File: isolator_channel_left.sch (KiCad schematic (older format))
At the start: 44 parts, among them U301 NE5532, U302 NE5532, U303 NE5532, U304 NE5532, U305 NE5532, U306 NE5532, U307 NE5532, U308 NE5532

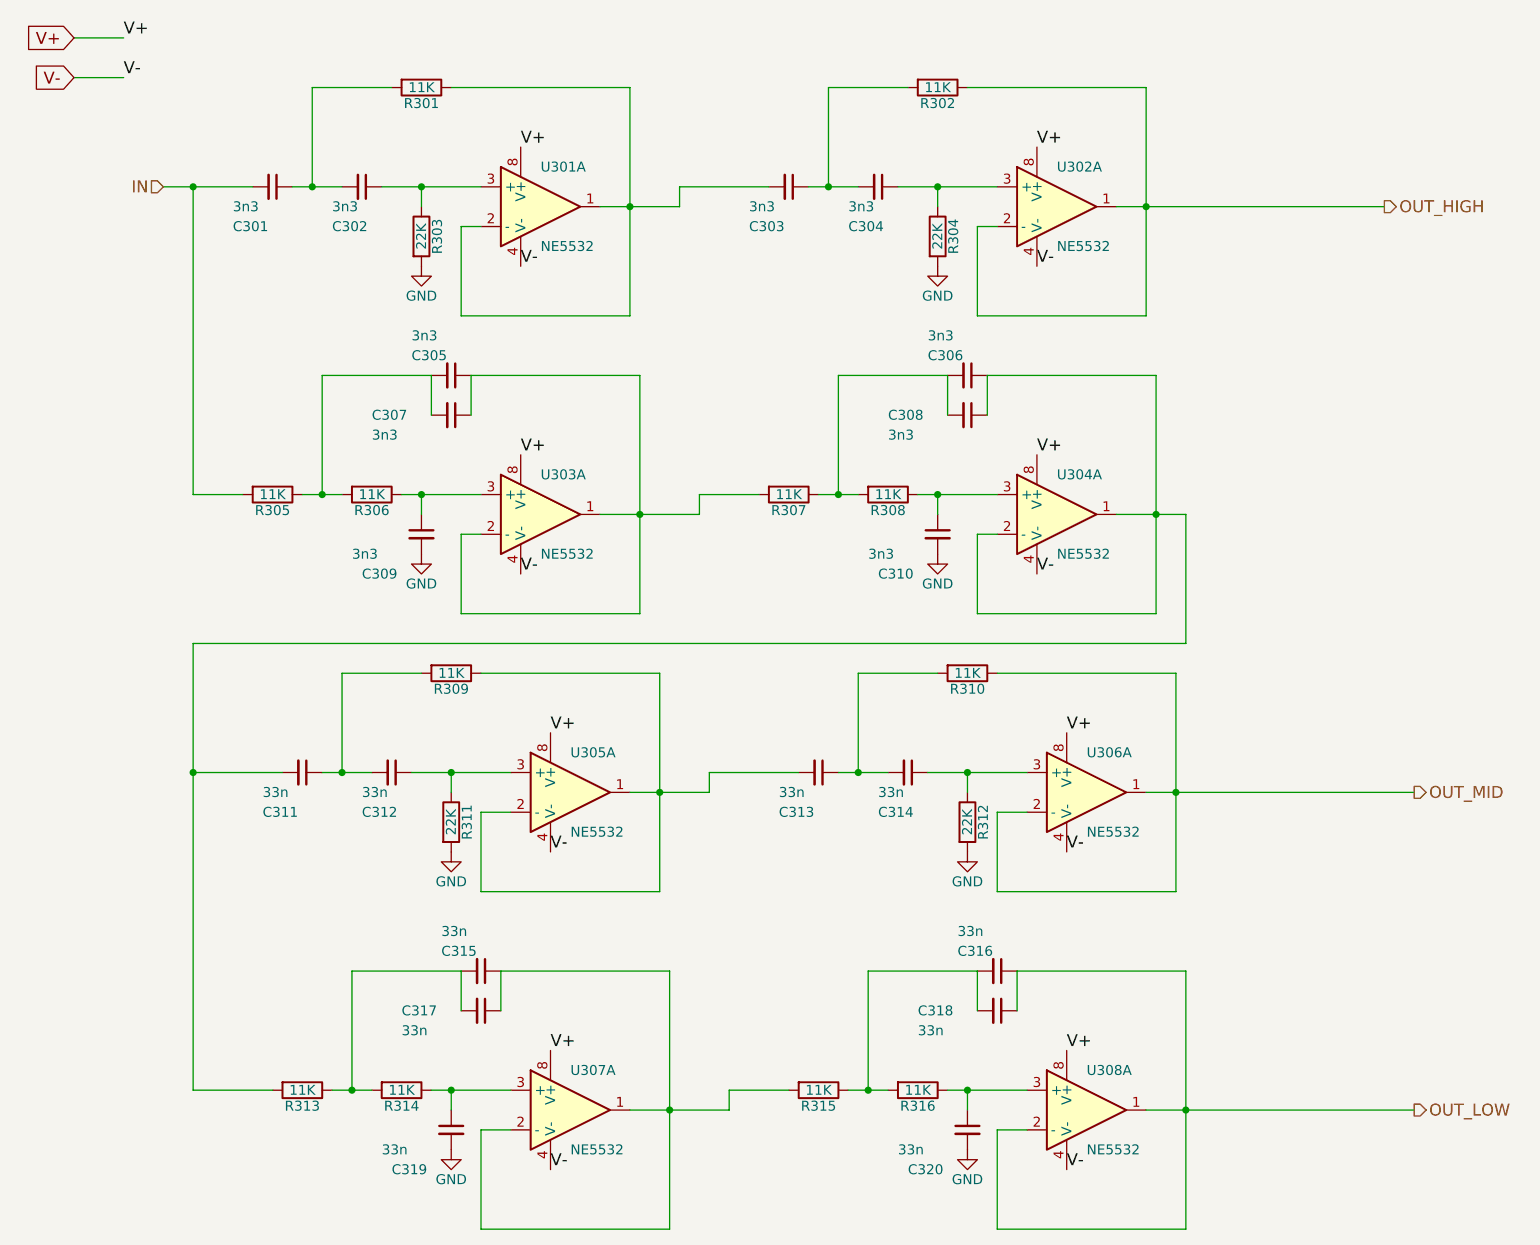
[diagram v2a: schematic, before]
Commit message: Updated components references and properties
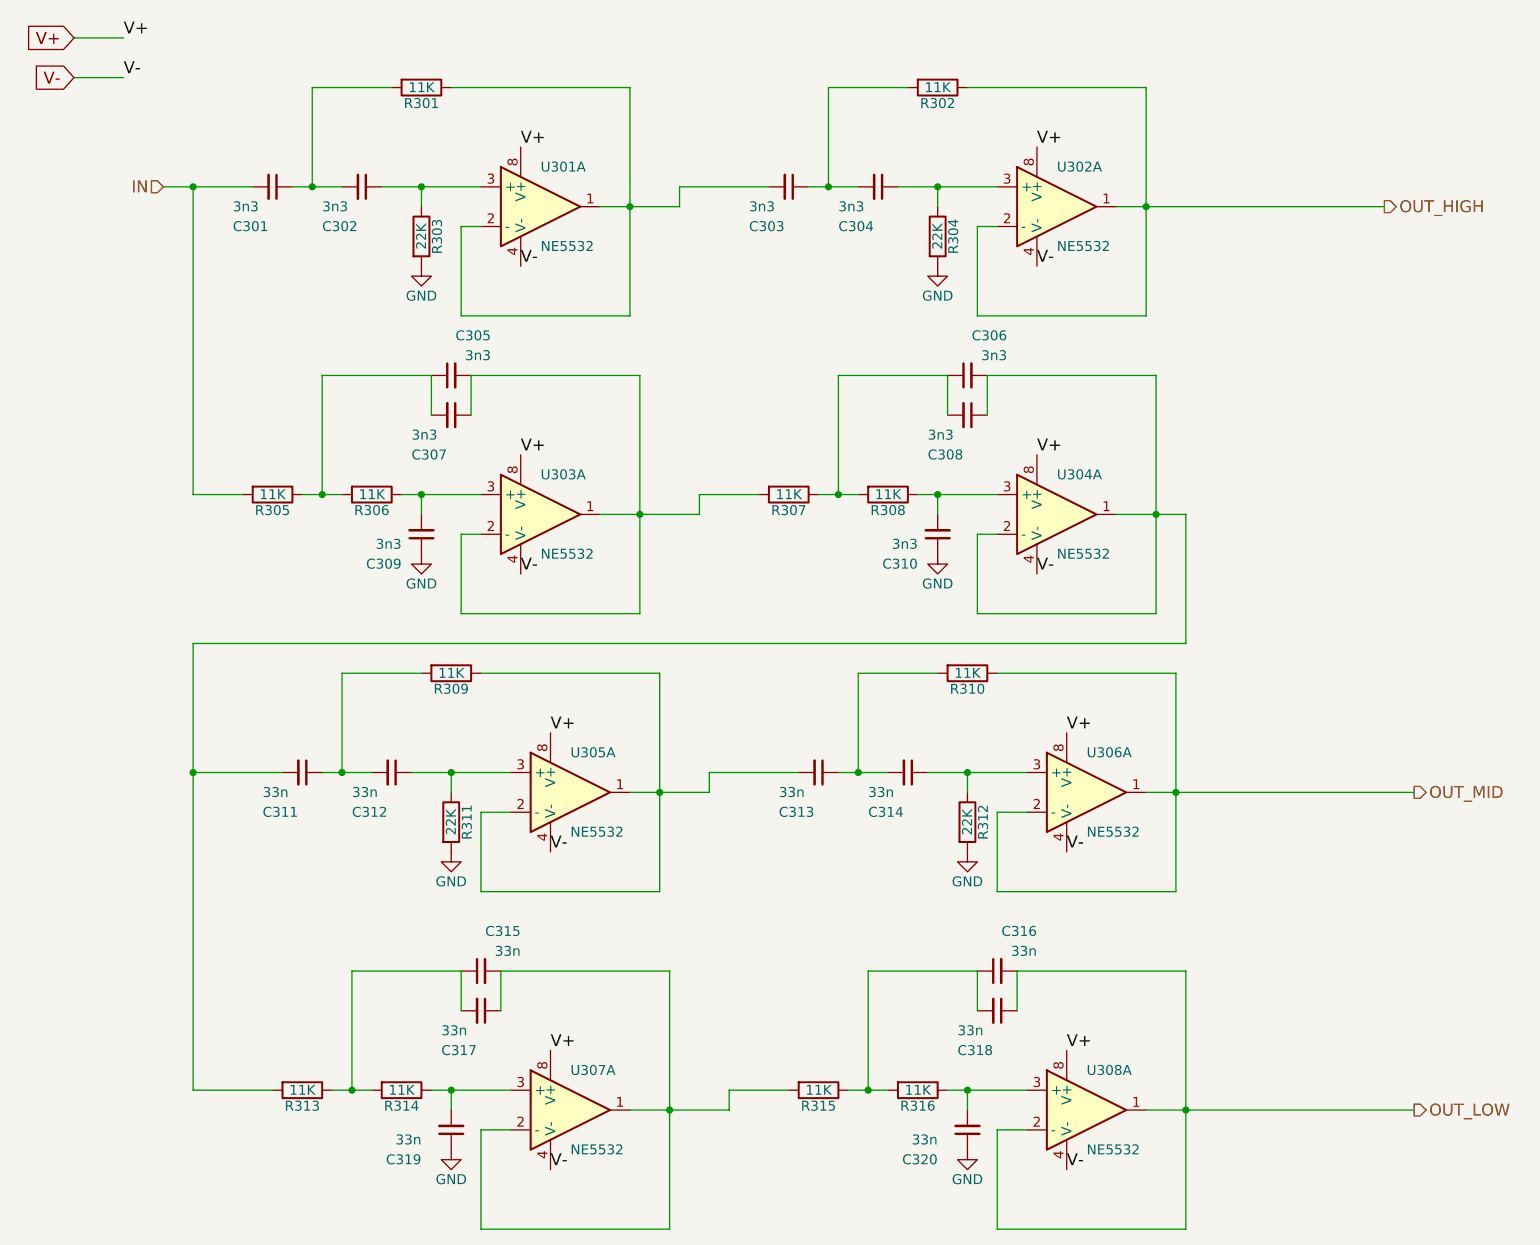
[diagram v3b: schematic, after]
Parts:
- removed C202, C203, C204, C205, C206, C207, C208, C209, C210: 3n3, Capacitors_THT:C_Rect_L7.0mm_W3.5mm_P5.00mm, symbol C_Small
- removed C211, C212, C213, C214, C215, C216, C217, C218, C219, C220: 33n, Capacitors_THT:C_Rect_L7.0mm_W3.5mm_P5.00mm, symbol C_Small
- removed R201, R202, R205, R206, R207, R208, R209, R210, R213, R214, R215, R216: 11K, Resistors_THT:R_Axial_DIN0204_L3.6mm_D1.6mm_P5.08mm_Horizontal, symbol R
- removed R204, R211, R212: 22K, Resistors_THT:R_Axial_DIN0204_L3.6mm_D1.6mm_P5.08mm_Horizontal, symbol R
- added C302, C303, C304, C305, C306, C307, C308, C309, C310: 3n3, Capacitors_THT:C_Rect_L7.0mm_W2.5mm_P5.00mm, symbol C_Small
- added C311, C312, C313, C314, C315, C316, C317, C318, C319, C320: 33n, Capacitors_THT:C_Rect_L7.0mm_W3.5mm_P5.00mm, symbol C_Small
- added R301, R302, R305, R306, R307, R308, R309, R310, R313, R314, R315, R316: 11K, Resistors_THT:R_Axial_DIN0204_L3.6mm_D1.6mm_P5.08mm_Horizontal, symbol R
- added R304, R311, R312: 22K, Resistors_THT:R_Axial_DIN0204_L3.6mm_D1.6mm_P5.08mm_Horizontal, symbol R
- C201: footprint Capacitors_THT:C_Rect_L7.0mm_W3.5mm_P5.00mm -> Capacitors_THT:C_Rect_L7.0mm_W2.5mm_P5.00mm; Description (none) -> Condensateurs à film 100volts 3300pF 5%; Distributor (none) -> Mouser; Distributor Part # (none) -> 80-R82EC1330JE50J; Manufacturer (none) -> Kemet; Mfg_Part_# (none) -> R82EC1330JE50J; Package (none) -> 2-THT
- R203: Description (none) -> Résistances à couche métallique - Trou traversant 1/3watts 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; Distributor (none) -> Mouser; Distributor Part # (none) -> 71-CCF50-J-22K; Manufacturer (none) -> Vishay / Dale; Mfg_Part_# (none) -> CCF5022K0JKR36; Package (none) -> DIN0204
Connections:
- net GND: now also C309.1, C310.1, C319.1, C320.1, R304.2, R311.2, R312.2
- net IN: now also R305.2
- net OUT_HIGH: now also R302.1
- net OUT_LOW: now also C316.2, C318.1
- net OUT_MID: now also R310.1
- net at R203.1, U301.3 (+): now also C302.1
- net at C201.1: now also C302.2, R301.2
- net at U302.3 (+): now also C304.1, R304.1
- net at U301.1, U301.2 (-): now also C303.2, R301.1
- net at U303.3 (+): now also C309.2, R306.1
- net at U303.1, U303.2 (-): now also C305.2, C307.1, R307.2
- net at U304.3 (+): now also C310.2, R308.1
- net at U304.1, U304.2 (-): now also C306.2, C308.1, C311.2, R313.2
- net at U305.3 (+): now also C312.1, R311.1
- net at U306.3 (+): now also C314.1, R312.1
- net at U305.1, U305.2 (-): now also C313.2, R309.1
- net at U307.3 (+): now also C319.2, R314.1
- net at U307.1, U307.2 (-): now also C315.2, C317.1, R315.2
- net at U308.3 (+): now also C320.2, R316.1
- new net: C303.1, C304.2, R302.2
- new net: C305.1, C307.2, R305.1, R306.2
- new net: C306.1, C308.2, R307.1, R308.2
- new net: C311.1, C312.2, R309.2
- new net: C313.1, C314.2, R310.2
- new net: C315.1, C317.2, R313.1, R314.2
- new net: C316.1, C318.2, R315.1, R316.2
